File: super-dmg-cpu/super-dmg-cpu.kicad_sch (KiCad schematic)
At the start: 59 parts, among them CN1 SCREEN, CN2 CART, CN3 EXT, CN4 BATTERY, P1 CART SHIELD GND PADS, P2 GND PAD, P3 GND PAD, P4 GND PAD, SW1 POWER_SW, U1 CPU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

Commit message: Version 1.7  - Rebranding  - Fix AA negative battery contact  - Add charger pads  - Made the power switch footprint compatible with a 3rd party switch  - Add experimental JACK board  - PCBWaaaaaaaaaaaaaaaaaaay
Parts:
- removed SW1: POWER_SW, dmg_lib:DMG_POWER_SWITCH, symbol kmc_lib:SW_DPST
- added H4: DMGB_CHRG_HEADER, kmc_lib:PAD_2.54_HYBRID_X3, symbol kmc_lib:DMGB_CHRG_HEADER
- added SW1: DPDT, kmc_lib:DMGB_POWER_SWITCH, symbol kmc_lib:DMGB_SW
- CN1: footprint kmc_lib:DMG_FPC_CONN -> dmg_lib:DMG_FPC_CONN
- CN3: renamed from H1; footprint kmc_lib:DMG_BATTERY_PADS -> dmg_lib:DMG_BATTERY_PADS
- G1: footprint eda-glyphs:kmc -> eda-glyphs:kmc_6mm
- renumbered CN3 to EXT1
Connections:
- net +BATT: now also H4.2 (BAT+), SW1.2 (VIN)
- net GND: now also H4.3 (GND), SW1.6 (GND), SW1.7 (SH)
- net RST: now also SW1.5 (RST)
- net SW_OUT: now also SW1.1 (VOUT)
- net VCC: now also H4.1 (VCC)
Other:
- title: DMG-01-B -> Super DMG CPU
- moved on the sheet: C1, C16, C17, C18, C19, CN2, CN4, D2, DA1, DA2, DA3, DA4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

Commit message: CPU: fix inverted L/R pins
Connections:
- net LOUT: now also C4.1; no longer C3.1
- net LPOT: now also VR1.2; no longer VR1.4
- net ROUT: now also C3.1; no longer C4.1
- net RPOT: now also VR1.4; no longer VR1.2
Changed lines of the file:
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@@
     (title "Super DMG CPU")
     (date "2022-12-03")
-    (rev "1.7")
+    (rev "1.8")
     (company "kmc")
   )
@@
     (effects (font (size 1.27 1.27)) (justify right bottom))
   )
-  (label "LPOT" (at 205.74 162.56 180)
-    (effects (font (size 1.27 1.27)) (justify right bottom))
-  )
   (label "RST" (at 226.06 99.06 180)
     (effects (font (size 1.27 1.27)) (justify right bottom))
@@
     (effects (font (size 1.27 1.27)) (justify left bottom))
   )
-  (label "RPOT" (at 205.74 187.96 180)
-    (effects (font (size 1.27 1.27)) (justify right bottom))
-  )
   (label "RST" (at 43.18 105.41 180)
     (effects (font (size 1.27 1.27)) (justify right bottom))
@@
     (effects (font (size 1.27 1.27)) (justify left bottom))
   )
-  (label "ROUT" (at 181.61 176.53 180)
-    (effects (font (size 1.27 1.27)) (justify right bottom))
-  )
   (label "CLK" (at 226.06 27.94 180)
     (effects (font (size 1.27 1.27)) (justify right bottom))
   )
+  (label "RPOT" (at 205.74 162.56 180)
+    (effects (font (size 1.27 1.27)) (justify right bottom))
+  )
   (label "RD" (at 110.49 53.34 0)
     (effects (font (size 1.27 1.27)) (justify left bottom))
@@
     (effects (font (size 1.27 1.27)) (justify right bottom))
   )
+  (label "ROUT" (at 181.61 171.45 180)
+    (effects (font (size 1.27 1.27)) (justify right bottom))
+  )
   (label "D3" (at 226.06 86.36 180)
     (effects (font (size 1.27 1.27)) (justify right bottom))
@@
     (effects (font (size 1.27 1.27)) (justify right bottom))
   )
-  (label "LOUT" (at 181.61 171.45 180)
-    (effects (font (size 1.27 1.27)) (justify right bottom))
-  )
   (label "D5" (at 110.49 43.18 0)
     (effects (font (size 1.27 1.27)) (justify left bottom))
@@
     (effects (font (size 1.27 1.27)) (justify right bottom))
   )
+  (label "LPOT" (at 205.74 187.96 180)
+    (effects (font (size 1.27 1.27)) (justify right bottom))
+  )
   (label "D3" (at 110.49 38.1 0)
     (effects (font (size 1.27 1.27)) (justify left bottom))
@@
     (effects (font (size 1.27 1.27)) (justify left bottom))
   )
+  (label "LOUT" (at 181.61 176.53 180)
+    (effects (font (size 1.27 1.27)) (justify right bottom))
+  )
   (label "EXT_IN" (at 262.89 34.29 180)

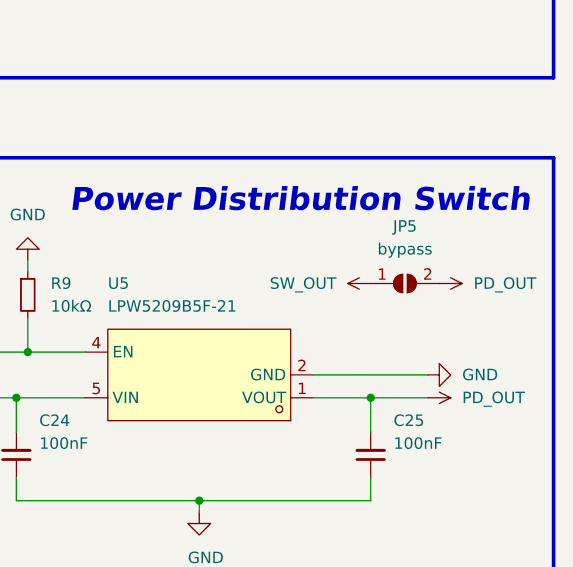
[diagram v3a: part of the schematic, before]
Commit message: Fixed the link port  - The link port footprint was flipped
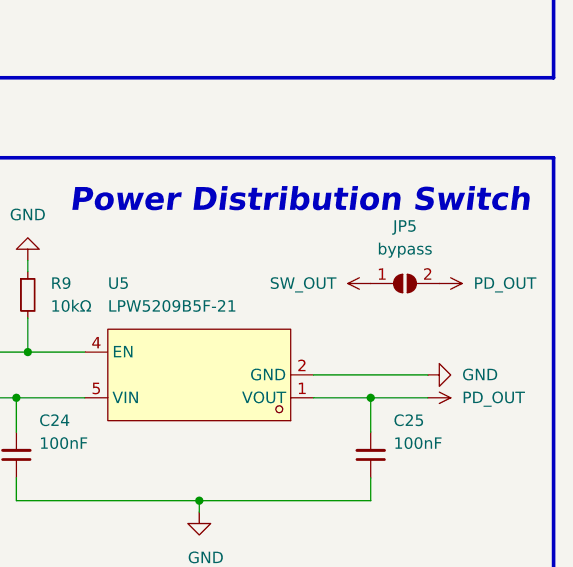
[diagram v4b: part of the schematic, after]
